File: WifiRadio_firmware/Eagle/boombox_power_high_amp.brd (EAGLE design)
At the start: 40.3 x 25.4 mm, 7 parts, among them IC1 7805TV, J1 POWER_JACKPTH, Q1 MJE3055

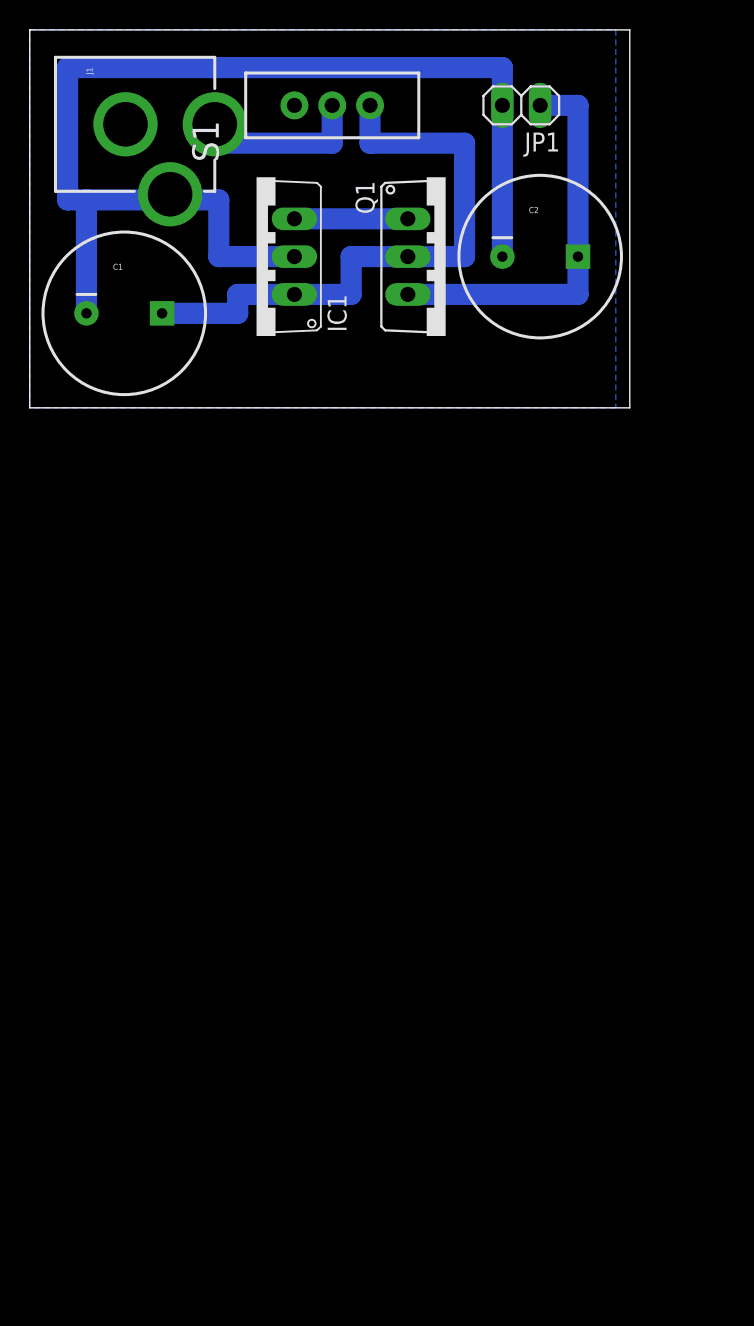
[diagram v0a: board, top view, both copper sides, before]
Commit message: Modified boards, changed pin asignment in lcd driver
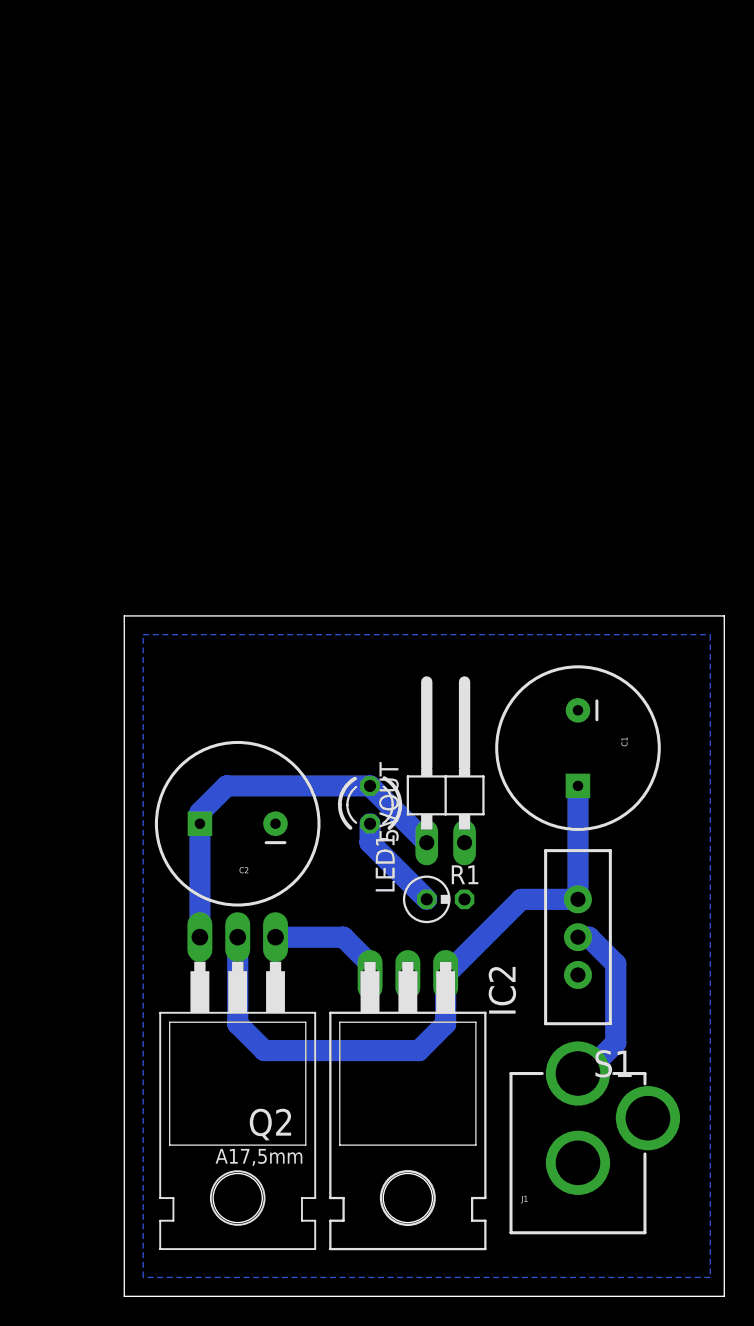
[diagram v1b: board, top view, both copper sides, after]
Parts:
- removed IC1: 7805TV, linear:TO220V
- removed JP1: (no value), pinhead:1X02
- removed Q1: MJE3055, transistor-power:TO220AV
- added 5VOUT: (no value), pinhead:1X02/90
- added IC2: 7805T, linear:TO220H
- added LED1: (no value), led:LED3MM
- added Q2: BD243, transistor-npn:TO220
- added R1: 330R, resistor:0309V
- moved J1 86.3 mm to (36.8, -3.81), turned to 0 degrees
- moved S1 58.3 mm to (36.8, 19.1), turned to 180 degrees
- moved C2 43.2 mm to (14.0, 26.7), turned to 180 degrees
- moved C1 42.2 mm to (36.8, 31.8), turned to 270 degrees
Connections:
- new net N$1: J1.GNDBREAK
- new net N$3: LED1.K, R1.1
- net 9V: now also IC2.1, Q2.2; no longer IC1.1, Q1.C
- net GND: now also 5VOUT.2, IC2.2, J1.GND, R1.2; no longer IC1.2, J1.GNDBREAK, JP1.2
- net N$2: now also 5VOUT.1, LED1.A, Q2.3; no longer JP1.1, Q1.E
- net VCC: now also IC2.3, Q2.1; no longer IC1.3, Q1.B
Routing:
- net GND: track 77.5 -> 0.00 mm
- net N$3: track 0.00 -> 6.66 mm
- net 9V: track 40.6 -> 43.2 mm
- net N$2: track 26.7 -> 25.9 mm
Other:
- board size 40.3 x 25.4 mm -> 40.3 x 45.7 mm
